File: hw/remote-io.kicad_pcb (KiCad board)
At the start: 2 copper layers, 80 parts, among them P1 CONN_01X02, P2 CONN_01X08, P3 CONN_01X08, P4 CONN_02X20, P5 CONN_01X08, P6 CONN_01X04, P7 CONN_01X02, P8 CONN_01X02, Q1 DMG2305UX, Q2 DMMT5401, U1 AP1506, U2 LP2992, U3 MCP3008, U4 CAT24C32, U5 MAX3488, U6 MCP2515, U7 ADM3054, Y1 Crystal

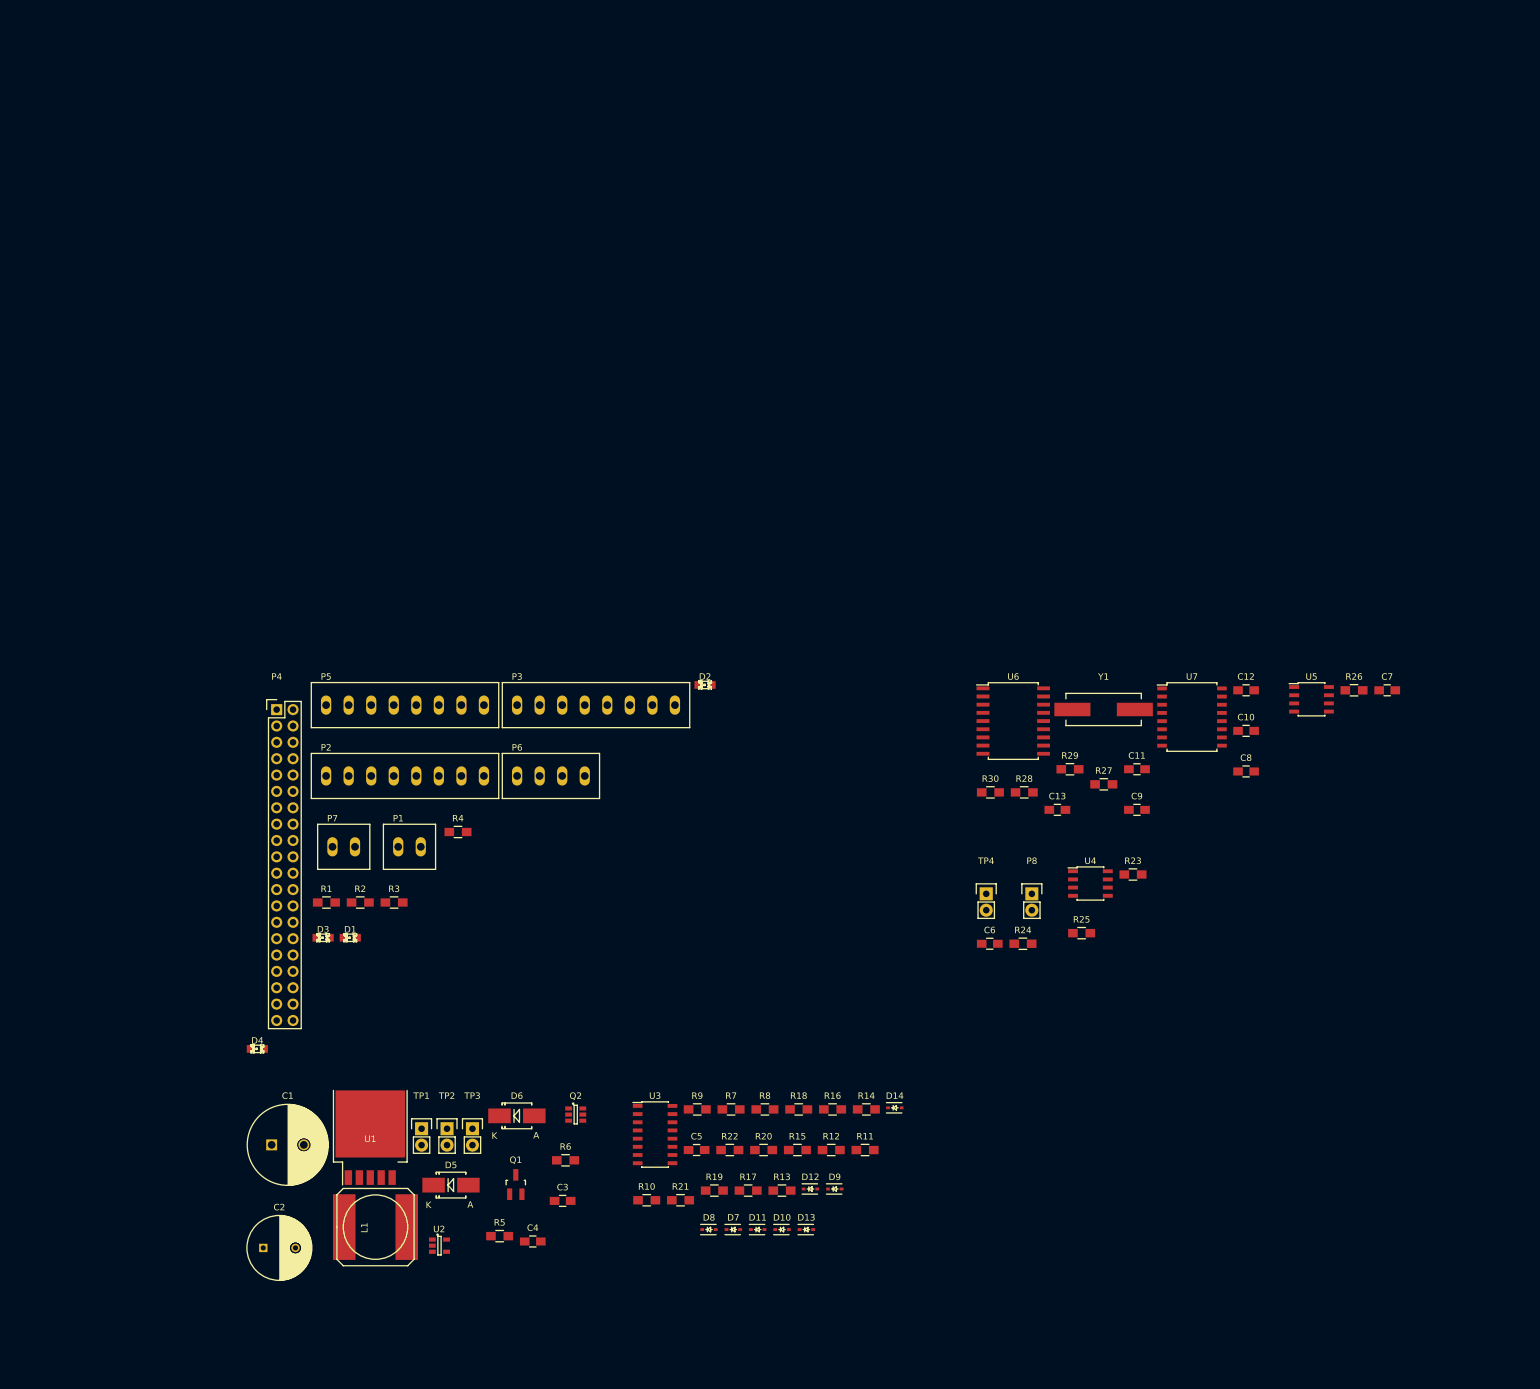
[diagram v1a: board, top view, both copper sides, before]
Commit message: Started fucking aroond with pcb layout. Power is tricky...
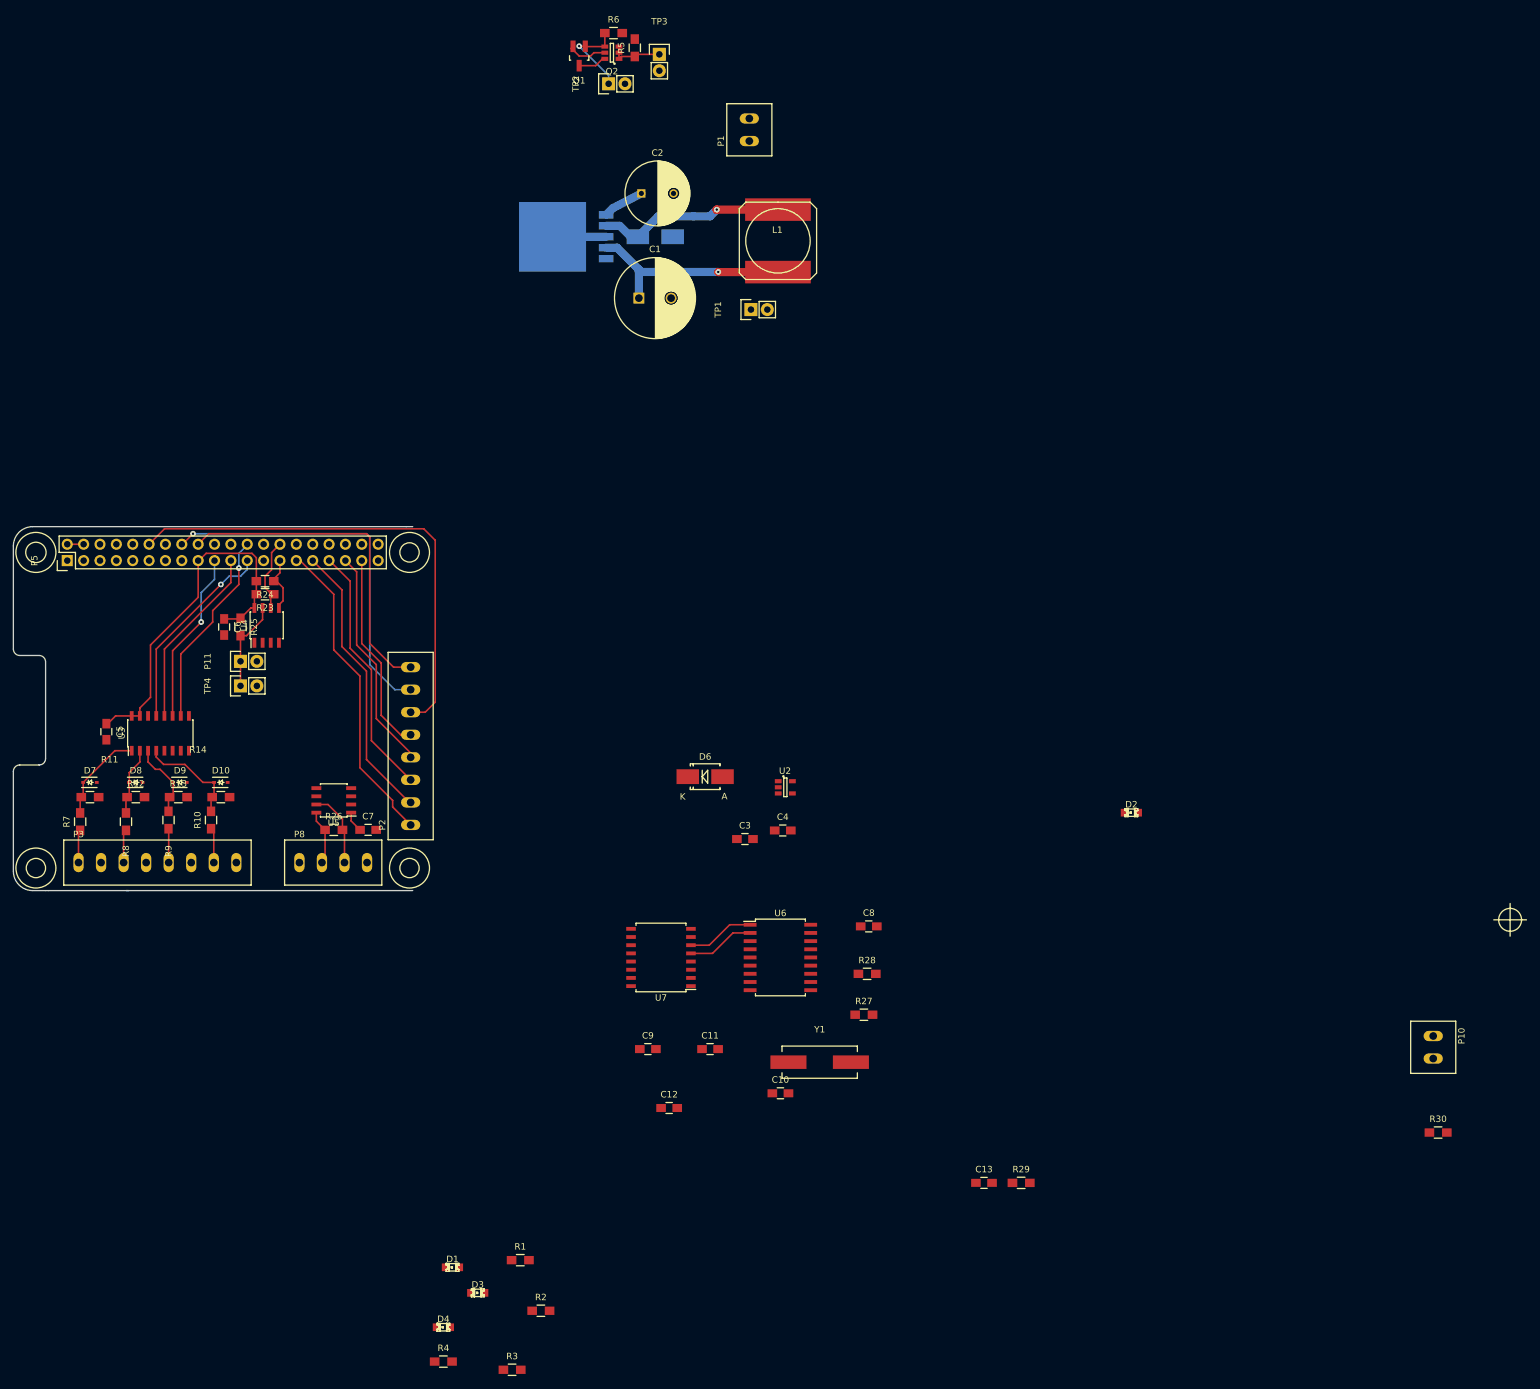
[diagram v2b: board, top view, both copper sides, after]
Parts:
- removed D11, D12, D13, D14: 3.9V, Diodes_SMD:SOD-323
- removed P4: CONN_02X20, Pin_Headers:Pin_Header_Straight_2x20
- removed P6: CONN_01X04, remote-io:OSTTE040104
- removed P7: CONN_01X02, remote-io:OSTTE020104
- removed R15, R16, R17, R18: 78.7k, Resistors_SMD:R_0805_HandSoldering
- removed R19, R20, R21, R22: 11.3k, Resistors_SMD:R_0805_HandSoldering
- added P10: CONN_01X02, remote-io:OSTTE020104, F.Cu at (249.4, 100.1)
- added P11: CONN_01X02, Pin_Headers:Pin_Header_Straight_1x02, F.Cu at (64.3, 41.9)
- D5, U1: moved to B.Cu
- P5: value CONN_01X08 -> CONN_02X20; footprint remote-io:OSTTE080104 -> Pin_Headers:Pin_Header_Straight_2x20
- P8: value CONN_01X02 -> CONN_01X04; footprint Pin_Headers:Pin_Header_Straight_1x02 -> remote-io:OSTTE040104
- moved R5 185.7 mm to (125.5, -53.3), turned to 90 degrees
- moved Q1 175.5 mm to (116.8, -52.1), turned to 180 degrees
- moved R6 175.2 mm to (122.2, -55.6)
- moved C2 173.9 mm to (126.5, -30.7)
- moved TP3 169.3 mm to (129.3, -52.3)
- moved L1 165.4 mm to (147.7, -23.4), turned to 270 degrees
- moved Q2 164.9 mm to (121.9, -52.6), turned to 180 degrees
- moved TP2 164.2 mm to (121.4, -47.8), turned to 90 degrees
- moved R26 159.9 mm to (78.7, 68.1)
- moved C7 159.7 mm to (84.1, 68.1)
- moved U5 152.6 mm to (78.7, 63.5), turned to 180 degrees
- moved D5 150.6 mm to (128.7, -24.0)
- moved U1 150.6 mm to (121.0, -24.0), turned to 270 degrees
- moved C1 143.3 mm to (126.1, -14.5)
- moved R23 141.6 mm to (68.1, 31.5), turned to 180 degrees
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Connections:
- C1 pad 2: Net-(C1-Pad2) -> GND
- C2 pad 2: Net-(C1-Pad2) -> GND
- C3 pad 1: Net-(C3-Pad1) -> +5VA
- C3 pad 2: Net-(C3-Pad2) -> GND
- C4 pad 2: Net-(C3-Pad2) -> GND
- D10 pad 2: Net-(D10-Pad2) -> GND
- D5 pad 2: Net-(C1-Pad2) -> GND
- D6 pad 2: Net-(C3-Pad1) -> +5VA
- D7 pad 2: Net-(D7-Pad2) -> GND
- D8 pad 2: Net-(D8-Pad2) -> GND
- D9 pad 2: Net-(D9-Pad2) -> GND
- P5 pad 1: /Battery Monitor/BAT_MEAS4 -> +3V3
- P5 pad 2: GND -> +5V
- P5 pad 3: /Battery Monitor/BAT_MEAS5 -> (no net)
- P5 pad 4: GND -> +5V
- P5 pad 5: /Battery Monitor/BAT_MEAS6 -> /CAN Controller and Transceiver/CAN_VSENSE
- P5 pad 7: /Battery Monitor/BAT_MEAS7 -> /CAN Controller and Transceiver/CAN_~INT
- P5 pad 8: GND -> (no net)
- P8 pad 1: Net-(P8-Pad1) -> +12V
- P8 pad 2: Net-(P8-Pad2) -> /RS-422 Level Converter/RS422_GPS
- R11 pad 2: Net-(D7-Pad2) -> GND
- R12 pad 2: Net-(D8-Pad2) -> GND
- R13 pad 2: Net-(D9-Pad2) -> GND
- R14 pad 2: Net-(D10-Pad2) -> GND
- R25 pad 2: Net-(P8-Pad1) -> Net-(P11-Pad1)
- R5 pad 2: Net-(R5-Pad2) -> GND
- R6 pad 2: Net-(R5-Pad2) -> GND
- TP4 pad 1: Net-(P8-Pad1) -> Net-(P11-Pad1)
- TP4 pad 2: Net-(P8-Pad2) -> GND
- U1 pad 5: Net-(C1-Pad2) -> GND
- U2 pad 5: Net-(C3-Pad1) -> +5VA
- U3 pad 5: /Battery Monitor/ADC_IN4 -> GND
- U3 pad 6: /Battery Monitor/ADC_IN5 -> GND
- U3 pad 7: /Battery Monitor/ADC_IN6 -> GND
- U3 pad 8: /Battery Monitor/ADC_IN7 -> GND
- U4 pad 7: Net-(P8-Pad1) -> Net-(P11-Pad1)
- U5 pad 5: Net-(U5-Pad5) -> (no net)
- U5 pad 6: Net-(U5-Pad6) -> (no net)
- U6 pad 10: Net-(U6-Pad10) -> (no net)
- U6 pad 11: Net-(U6-Pad11) -> (no net)
- U6 pad 3: Net-(U6-Pad3) -> (no net)
- U6 pad 4: Net-(U6-Pad4) -> (no net)
- U6 pad 5: Net-(U6-Pad5) -> (no net)
- U6 pad 6: Net-(U6-Pad6) -> (no net)
- U7 pad 1: Net-(U7-Pad1) -> (no net)
- U7 pad 10: Net-(U7-Pad10) -> (no net)
- U7 pad 14: Net-(U7-Pad14) -> (no net)
- U7 pad 15: Net-(U7-Pad15) -> (no net)
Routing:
- net /SW_IN5: track 0.00 -> 75.7 mm
- net +3V3: track 0.00 -> 59.9 mm
- net /SW_IN6: track 0.00 -> 57.8 mm, vias 0 -> 1
- net /SW_IN7: track 0.00 -> 51.9 mm
- net /SW_IN0: track 0.00 -> 48.7 mm
- net /SW_IN1: track 0.00 -> 44.0 mm
- net /SW_IN2: track 0.00 -> 39.3 mm
- net /Power/V_REG: track 0.00 -> 37.3 mm, vias 0 -> 1
- net /SW_IN3: track 0.00 -> 34.7 mm
- net /SW_IN4: track 0.00 -> 31.1 mm
- net /Battery Monitor/ADC_CLK: track 0.00 -> 31.0 mm, vias 0 -> 1
- net /Battery Monitor/ADC_~CS~/SHDN: track 0.00 -> 31.0 mm, vias 0 -> 1
- net Net-(D5-Pad1): track 0.00 -> 29.7 mm, vias 0 -> 1
- net /Battery Monitor/ADC_DOUT: track 0.00 -> 28.4 mm
- net /Battery Monitor/ADC_DIN: track 0.00 -> 26.8 mm, vias 0 -> 1
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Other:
- board outline added: 62 x 56.5 mm
- net class 12v added: clearance 0.512, trace_width 0.512, via_dia 0.889, via_drill 0.381
- net class Default: clearance 0.2 -> 0.0254; trace_width 0.25 -> 0.254; via_dia 0.6 -> 0.889; via_drill 0.4 -> 0.381
- net class Rf added: clearance 0.254, trace_width 1, via_dia 0.889, via_drill 0.381
- net class alim added: clearance 0.254, trace_width 0.512, via_dia 0.889, via_drill 0.381
- rule trace_clearance: 0.2 -> 0.0254
- rule trace_min: 0.2 -> 0.254
- rule via_min_drill: 0.3 -> 0.381
- rule via_min_size: 0.4 -> 0.889

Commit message: All parts in hat-spec-size board
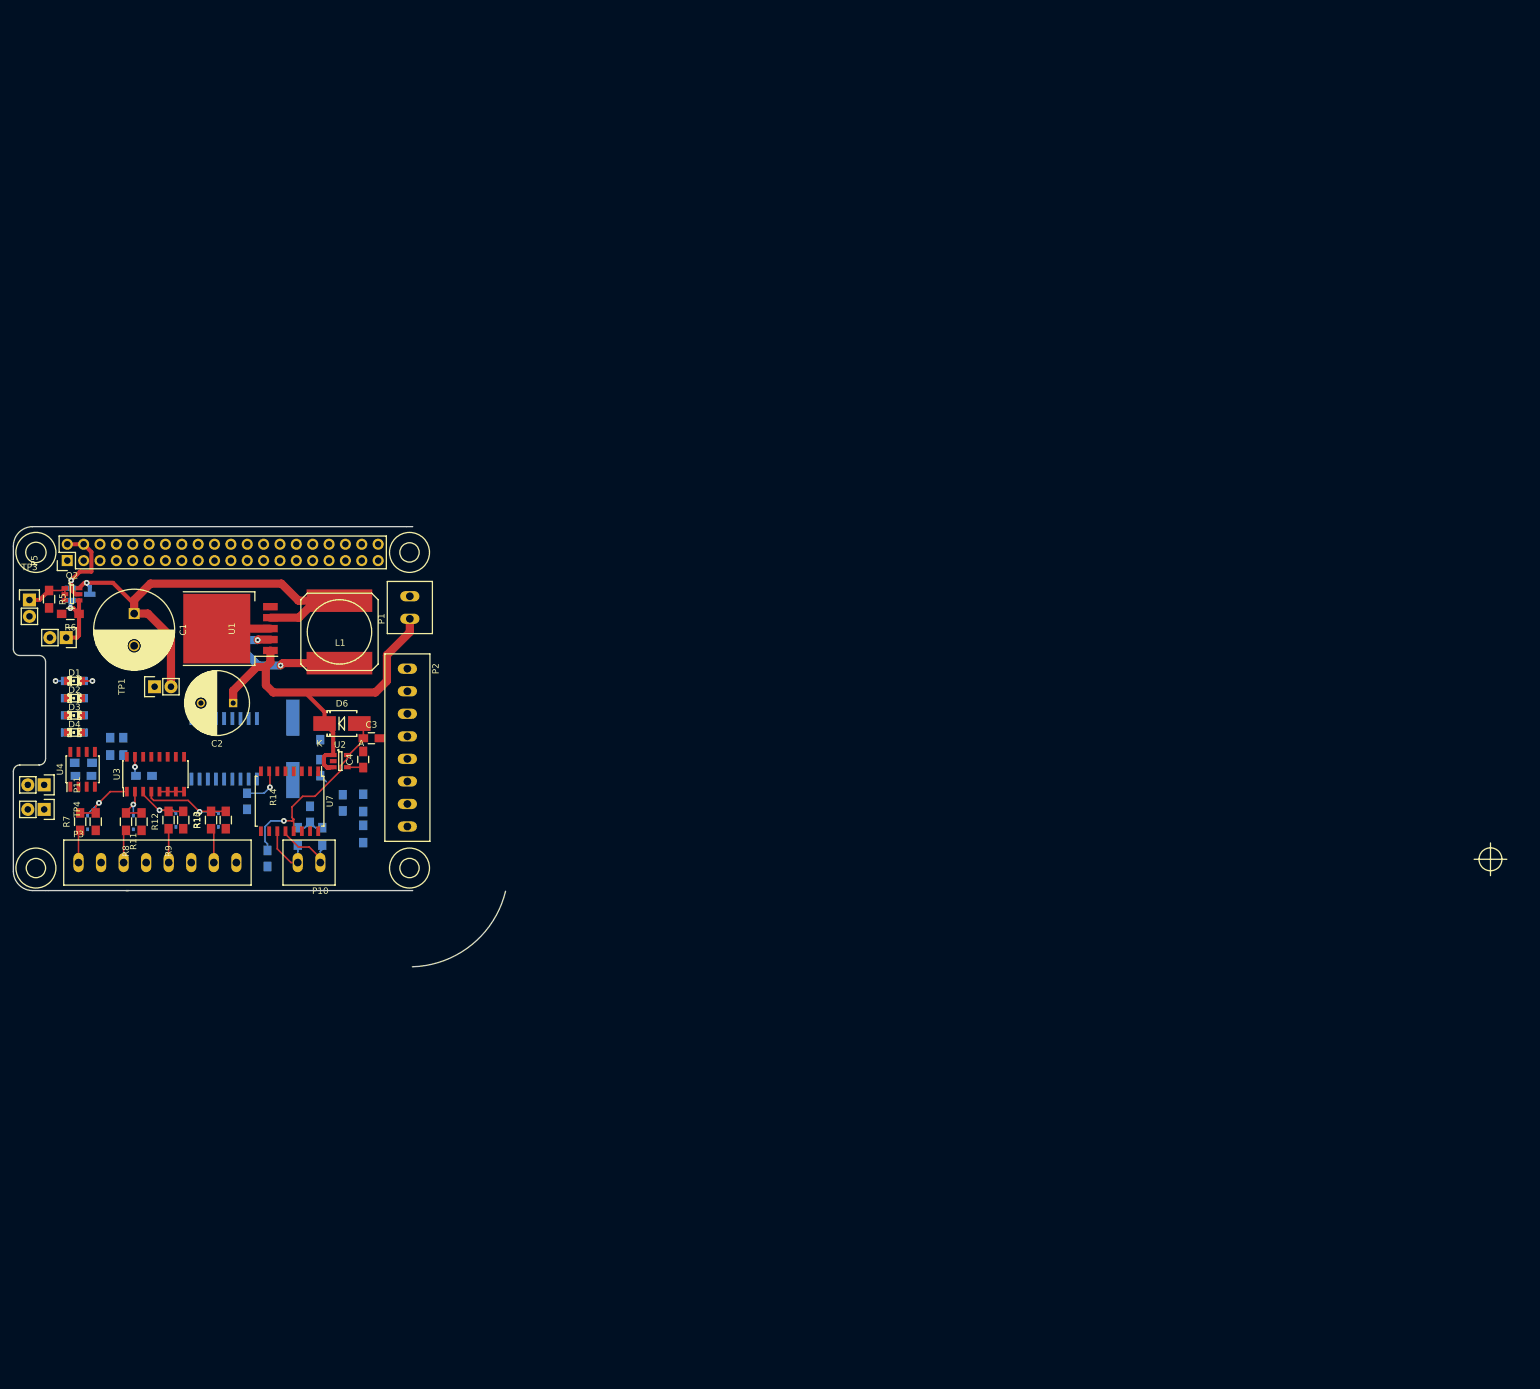
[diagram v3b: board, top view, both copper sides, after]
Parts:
- removed C7: 0.1uF, Capacitors_SMD:C_0805_HandSoldering
- removed P8: CONN_01X04, remote-io:OSTTE040104
- removed R26: 120, Resistors_SMD:R_0805_HandSoldering
- removed U5: MAX3488, Housings_SOIC:SOIC-8_3.9x4.9mm_Pitch1.27mm
- C10, C11, C12, C13, C5, C6, C8, C9, D10, D7, D8, D9, Q1, R1, R2, R23, R24, R25, R27, R28, R29, R3, R30, R4, U6, Y1: moved to B.Cu
- U1: moved to F.Cu
- moved R30 182.9 mm to (73.2, 69.1), turned to 270 degrees
- moved P10 174.9 mm to (76.7, 73.2), turned to 180 degrees
- moved D2 165.0 mm to (38.5, 47.6)
- moved TP3 129.4 mm to (31.5, 32.4)
- moved R5 124.9 mm to (34.5, 32.3), turned to 270 degrees
- moved R6 123.5 mm to (37.8, 34.5), turned to 180 degrees
- moved R3 122.2 mm to (38.5, 50.3)
- moved R29 121.1 mm to (77.0, 69.1), turned to 90 degrees
- moved TP2 120.3 mm to (37.2, 38.2), turned to 270 degrees
- moved R2 119.5 mm to (38.5, 47.6)
- moved C13 119.3 mm to (75.1, 65.7), turned to 90 degrees
- moved Q2 118.7 mm to (38.1, 31.5), turned to 0 degrees
- moved Q1 114.0 mm to (39.4, 31.5), turned to 90 degrees
- moved R1 113.5 mm to (38.5, 45.0)
- moved R4 113.2 mm to (38.5, 53.0)
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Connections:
- P2 pad 2: /SW_IN1 -> GND
- P2 pad 3: /SW_IN2 -> /SW_IN1
- P2 pad 4: /SW_IN3 -> GND
- P2 pad 5: /SW_IN4 -> /SW_IN2
- P2 pad 6: /SW_IN5 -> GND
- P2 pad 7: /SW_IN6 -> /SW_IN3
- P2 pad 8: /SW_IN7 -> GND
- P5 pad 10: /RS-422 Level Converter/RX_GPS -> (no net)
- P5 pad 12: /SW_IN5 -> (no net)
- P5 pad 16: /SW_IN6 -> (no net)
- P5 pad 18: /SW_IN7 -> (no net)
- P5 pad 37: /SW_IN4 -> (no net)
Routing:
- net /SW_IN5: track 75.7 -> 0.00 mm
- net +12V: track 6.45 -> 66.2 mm
- net /SW_IN6: track 57.8 -> 0.00 mm, vias 1 -> 0
- net /SW_IN7: track 51.9 -> 0.00 mm
- net +3V3: track 59.9 -> 9.75 mm, vias 0 -> 2
- net /SW_IN0: track 48.7 -> 0.00 mm
- net /SW_IN1: track 44.0 -> 0.00 mm
- net /SW_IN2: track 39.3 -> 0.00 mm
- net /Power/V_REG: track 37.3 -> 76.6 mm
- net /SW_IN3: track 34.7 -> 0.00 mm
- net +5VA: track 0.00 -> 31.7 mm, vias 0 -> 1
- net /SW_IN4: track 31.1 -> 0.00 mm
- net /Battery Monitor/ADC_CLK: track 31.0 -> 0.00 mm, vias 1 -> 0
- net /Battery Monitor/ADC_~CS~/SHDN: track 31.0 -> 0.19 mm, vias 1 -> 0
- net /Battery Monitor/ADC_DOUT: track 28.4 -> 0.00 mm
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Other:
- board size 62 x 56.5 mm -> 76.4 x 68.3 mm
